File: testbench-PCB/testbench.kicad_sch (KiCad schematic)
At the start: 0 parts

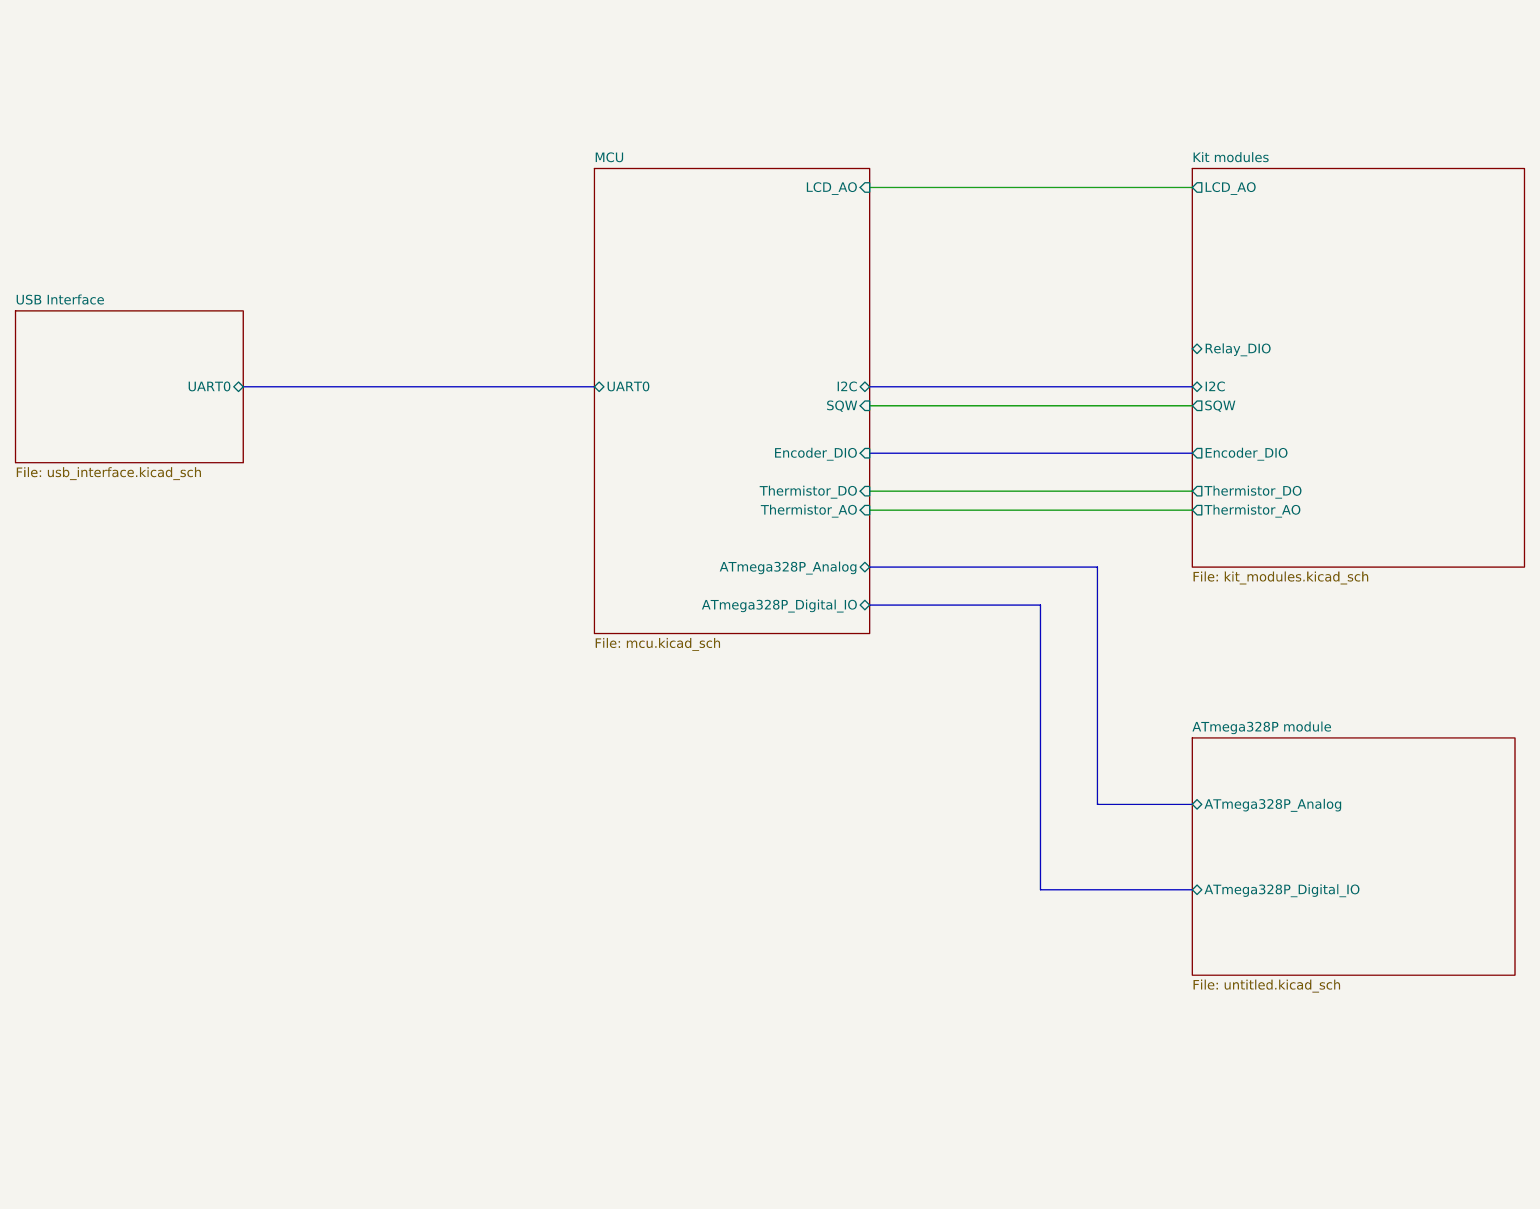
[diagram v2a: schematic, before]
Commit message: Finished connection between modules and MCU.
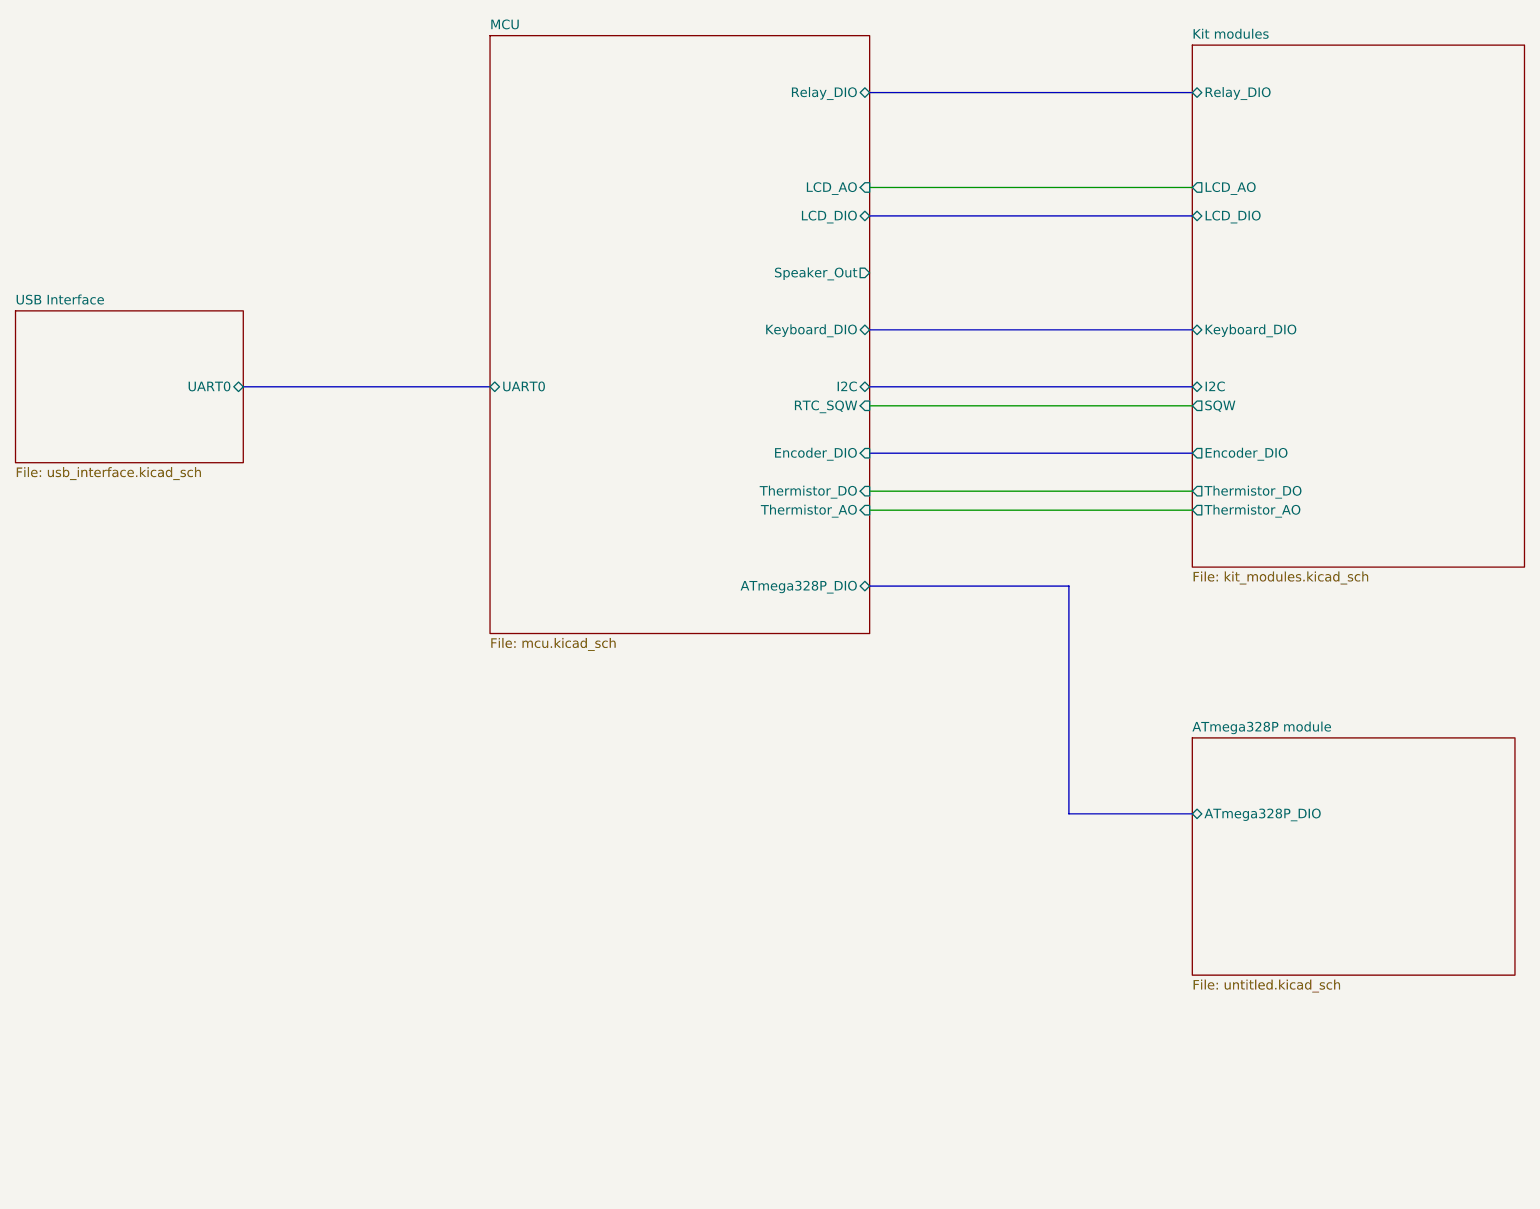
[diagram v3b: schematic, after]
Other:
- sheet ATmega328P module ports: added ATmega328P_DIO; removed ATmega328P_Analog, ATmega328P_Digital_IO
- sheet Kit modules ports: added Keyboard_DIO, LCD_DIO; removed none
- sheet MCU ports: added ATmega328P_DIO, Keyboard_DIO, LCD_DIO, RTC_SQW, Relay_DIO, Speaker_Out; removed ATmega328P_Analog, ATmega328P_Digital_IO, SQW
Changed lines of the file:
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@@
     (stroke (width 0) (type default))
   )
-  (bus (pts (xy 64.77 71.12) (xy 111.76 71.12))
+  (bus (pts (xy 175.26 128.27) (xy 191.77 128.27))
     (stroke (width 0) (type default))
   )
-  (bus (pts (xy 171.45 138.43) (xy 191.77 138.43))
+  (bus (pts (xy 64.77 71.12) (xy 97.79 71.12))
+    (stroke (width 0) (type default))
+  )
+  (bus (pts (xy 148.59 63.5) (xy 191.77 63.5))
     (stroke (width 0) (type default))
   )
@@
     (stroke (width 0) (type default))
   )
-  (bus (pts (xy 171.45 100.33) (xy 171.45 138.43))
-    (stroke (width 0) (type default))
-  )
-  (bus (pts (xy 148.59 95.25) (xy 179.07 95.25))
+  (bus (pts (xy 148.59 48.26) (xy 191.77 48.26))
     (stroke (width 0) (type default))
   )
   (wire (pts (xy 148.59 85.09) (xy 191.77 85.09))
-    (stroke (width 0) (type default))
-  )
-  (bus (pts (xy 179.07 95.25) (xy 179.07 127))
     (stroke (width 0) (type default))
   )
@@
     (stroke (width 0) (type default))
   )
-  (bus (pts (xy 179.07 127) (xy 191.77 127))
+  (bus (pts (xy 148.59 31.75) (xy 191.77 31.75))
+    (stroke (width 0) (type default))
+  )
+  (bus (pts (xy 175.26 97.79) (xy 175.26 128.27))
     (stroke (width 0) (type default))
   )
@@
     (stroke (width 0) (type default))
   )
-  (bus (pts (xy 148.59 100.33) (xy 171.45 100.33))
+  (bus (pts (xy 148.59 97.79) (xy 175.26 97.79))
     (stroke (width 0) (type default))
   )
-  (sheet (at 111.76 41.91) (size 36.83 62.23) (fields_autoplaced)
+  (sheet (at 97.79 24.13) (size 50.8 80.01) (fields_autoplaced)
     (stroke (width 0.1524) (type solid))
     (fill (color 255 229 191 1.0000))
-    (property "Sheetname" "MCU" (at 111.76 41.1984 0)
+    (property "Sheetname" "MCU" (at 97.79 23.4184 0)
       (effects (font (size 1.27 1.27)) (justify left bottom))
     )
-    (property "Sheetfile" "mcu.kicad_sch" (at 111.76 104.7246 0)
+    (property "Sheetfile" "mcu.kicad_sch" (at 97.79 104.7246 0)
       (effects (font (size 1.27 1.27)) (justify left top))
     )
-    (pin "UART0" bidirectional (at 111.76 71.12 180)
+    (pin "UART0" bidirectional (at 97.79 71.12 180)
       (effects (font (size 1.27 1.27)) (justify left))
     )
     (pin "I2C" bidirectional (at 148.59 71.12 0)
-      (effects (font (size 1.27 1.27)) (justify right))
-    )
-    (pin "SQW" input (at 148.59 73.66 0)
-      (effects (font (size 1.27 1.27)) (justify right))
-    )
-    (pin "ATmega328P_Analog" bidirectional (at 148.59 95.25 0)
-      (effects (font (size 1.27 1.27)) (justify right))
-    )
-    (pin "ATmega328P_Digital_IO" bidirectional (at 148.59 100.33 0)
       (effects (font (size 1.27 1.27)) (justify right))
     )
@@
     )
     (pin "Thermistor_DO" input (at 148.59 85.09 0)
+      (effects (font (size 1.27 1.27)) (justify right))
+    )
+    (pin "Keyboard_DIO" bidirectional (at 148.59 63.5 0)
+      (effects (font (size 1.27 1.27)) (justify right))
+    )
+    (pin "LCD_DIO" bidirectional (at 148.59 48.26 0)
+      (effects (font (size 1.27 1.27)) (justify right))
+    )
+    (pin "Speaker_Out" output (at 148.59 55.88 0)
+      (effects (font (size 1.27 1.27)) (justify right))
+    )
+    (pin "Relay_DIO" bidirectional (at 148.59 31.75 0)
+      (effects (font (size 1.27 1.27)) (justify right))
+    )
+    (pin "ATmega328P_DIO" bidirectional (at 148.59 97.79 0)
+      (effects (font (size 1.27 1.27)) (justify right))
+    )
+    (pin "RTC_SQW" input (at 148.59 73.66 0)
       (effects (font (size 1.27 1.27)) (justify right))
     )
@@
       (effects (font (size 1.27 1.27)) (justify left top))
     )
-    (pin "ATmega328P_Analog" bidirectional (at 191.77 127 180)
-      (effects (font (size 1.27 1.27)) (justify left))
-    )
-    (pin "ATmega328P_Digital_IO" bidirectional (at 191.77 138.43 180)
+    (pin "ATmega328P_DIO" bidirectional (at 191.77 128.27 180)
       (effects (font (size 1.27 1.27)) (justify left))
     )
@@
     )
   )
-  (sheet (at 191.77 41.91) (size 44.45 53.34) (fields_autoplaced)
+  (sheet (at 191.77 25.4) (size 44.45 69.85) (fields_autoplaced)
     (stroke (width 0.1524) (type solid))
     (fill (color 255 229 191 1.0000))
-    (property "Sheetname" "Kit modules" (at 191.77 41.1984 0)
+    (property "Sheetname" "Kit modules" (at 191.77 24.6884 0)
       (effects (font (size 1.27 1.27)) (justify left bottom))
     )
     (property "Sheetfile" "kit_modules.kicad_sch" (at 191.77 95.8346 0)
       (effects (font (size 1.27 1.27)) (justify left top))
-    )
-    (pin "Relay_DIO" bidirectional (at 191.77 66.04 180)
-      (effects (font (size 1.27 1.27)) (justify left))
     )
     (pin "I2C" bidirectional (at 191.77 71.12 180)
@@
       (effects (font (size 1.27 1.27)) (justify left))
     )
+    (pin "Keyboard_DIO" bidirectional (at 191.77 63.5 180)
+      (effects (font (size 1.27 1.27)) (justify left))
+    )
+    (pin "LCD_DIO" bidirectional (at 191.77 48.26 180)
+      (effects (font (size 1.27 1.27)) (justify left))
+    )
+    (pin "Relay_DIO" bidirectional (at 191.77 31.75 180)
+      (effects (font (size 1.27 1.27)) (justify left))
+    )

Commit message: Changed naming convention.
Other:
- sheet ATmega328P module ports: added DUT[0..20]; removed ATmega328P_DIO
- sheet Kit modules ports: added KEY_D[0..7], LCD_D[0..6], RTC_SQW, {Encoder_DIO}, {I2C}, {RELAY_IO}; removed Encoder_DIO, I2C, Keyboard_DIO, LCD_DIO, Relay_DIO, SQW
- sheet MCU ports: added DUT[0..20], KEY_D[0..7], LCD_D[0..6], {Encoder_DIO}, {I2C}, {RELAY_IO}, {UART0}; removed ATmega328P_DIO, Encoder_DIO, I2C, Keyboard_DIO, LCD_DIO, Relay_DIO, UART0
- sheet USB Interface ports: added {UART0}; removed UART0
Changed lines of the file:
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@@
 (kicad_sch (version 20230121) (generator eeschema)
   (paper "A4")
-  (bus (pts (xy 148.59 80.01) (xy 191.77 80.01))
+  (wire (pts (xy 191.77 74.93) (xy 148.59 74.93))
     (stroke (width 0) (type default))
   )
-  (bus (pts (xy 175.26 128.27) (xy 191.77 128.27))
+  (bus (pts (xy 148.59 50.8) (xy 191.77 50.8))
     (stroke (width 0) (type default))
   )
-  (bus (pts (xy 64.77 71.12) (xy 97.79 71.12))
+  (bus (pts (xy 148.59 43.815) (xy 191.77 43.815))
     (stroke (width 0) (type default))
   )
-  (bus (pts (xy 148.59 63.5) (xy 191.77 63.5))
+  (bus (pts (xy 148.59 97.79) (xy 170.18 97.79))
     (stroke (width 0) (type default))
   )
-  (wire (pts (xy 148.59 73.66) (xy 191.77 73.66))
+  (wire (pts (xy 148.59 35.56) (xy 191.77 35.56))
     (stroke (width 0) (type default))
   )
-  (bus (pts (xy 148.59 48.26) (xy 191.77 48.26))
+  (wire (pts (xy 148.59 80.645) (xy 191.77 80.645))
     (stroke (width 0) (type default))
   )
-  (wire (pts (xy 148.59 85.09) (xy 191.77 85.09))
+  (bus (pts (xy 64.77 74.93) (xy 97.79 74.93))
     (stroke (width 0) (type default))
   )
-  (wire (pts (xy 148.59 87.63) (xy 191.77 87.63))
+  (bus (pts (xy 170.18 128.27) (xy 191.77 128.27))
     (stroke (width 0) (type default))
   )
-  (wire (pts (xy 148.59 44.45) (xy 191.77 44.45))
+  (bus (pts (xy 170.18 97.79) (xy 170.18 128.27))
     (stroke (width 0) (type default))
   )
-  (bus (pts (xy 148.59 31.75) (xy 191.77 31.75))
+  (bus (pts (xy 148.59 67.945) (xy 191.77 67.945))
     (stroke (width 0) (type default))
   )
-  (bus (pts (xy 175.26 97.79) (xy 175.26 128.27))
+  (bus (pts (xy 148.59 57.15) (xy 191.77 57.15))
     (stroke (width 0) (type default))
   )
-  (bus (pts (xy 148.59 71.12) (xy 191.77 71.12))
+  (bus (pts (xy 191.77 90.17) (xy 148.59 90.17))
     (stroke (width 0) (type default))
   )
-  (bus (pts (xy 148.59 97.79) (xy 175.26 97.79))
+  (wire (pts (xy 148.59 33.02) (xy 191.77 33.02))
     (stroke (width 0) (type default))
   )
@@
       (effects (font (size 1.27 1.27)) (justify left top))
     )
-    (pin "UART0" bidirectional (at 97.79 71.12 180)
+    (pin "{UART0}" bidirectional (at 97.79 74.93 180)
       (effects (font (size 1.27 1.27)) (justify left))
     )
-    (pin "I2C" bidirectional (at 148.59 71.12 0)
+    (pin "LCD_D[0..6]" bidirectional (at 148.59 57.15 0)
       (effects (font (size 1.27 1.27)) (justify right))
     )
-    (pin "Encoder_DIO" input (at 148.59 80.01 0)
+    (pin "KEY_D[0..7]" bidirectional (at 148.59 50.8 0)
       (effects (font (size 1.27 1.27)) (justify right))
     )
-    (pin "LCD_AO" input (at 148.59 44.45 0)
+    (pin "{I2C}" bidirectional (at 148.59 43.815 0)
       (effects (font (size 1.27 1.27)) (justify right))
     )
-    (pin "Thermistor_AO" input (at 148.59 87.63 0)
+    (pin "Speaker_Out" output (at 148.59 28.575 0)
       (effects (font (size 1.27 1.27)) (justify right))
     )
-    (pin "Thermistor_DO" input (at 148.59 85.09 0)
+    (pin "{RELAY_IO}" bidirectional (at 148.59 67.945 0)
       (effects (font (size 1.27 1.27)) (justify right))
     )
-    (pin "Keyboard_DIO" bidirectional (at 148.59 63.5 0)
+    (pin "RTC_SQW" input (at 148.59 80.645 0)
       (effects (font (size 1.27 1.27)) (justify right))
     )
-    (pin "LCD_DIO" bidirectional (at 148.59 48.26 0)
+    (pin "DUT[0..20]" bidirectional (at 148.59 97.79 0)
       (effects (font (size 1.27 1.27)) (justify right))
     )
-    (pin "Speaker_Out" output (at 148.59 55.88 0)
+    (pin "{Encoder_DIO}" input (at 148.59 90.17 0)
       (effects (font (size 1.27 1.27)) (justify right))
     )
-    (pin "Relay_DIO" bidirectional (at 148.59 31.75 0)
+    (pin "Thermistor_DO" input (at 148.59 33.02 0)
       (effects (font (size 1.27 1.27)) (justify right))
     )
-    (pin "ATmega328P_DIO" bidirectional (at 148.59 97.79 0)
+    (pin "Thermistor_AO" input (at 148.59 35.56 0)
       (effects (font (size 1.27 1.27)) (justify right))
     )
-    (pin "RTC_SQW" input (at 148.59 73.66 0)
+    (pin "LCD_AO" input (at 148.59 74.93 0)
       (effects (font (size 1.27 1.27)) (justify right))
     )
@@
       (effects (font (size 1.27 1.27)) (justify left top))
     )
-    (pin "ATmega328P_DIO" bidirectional (at 191.77 128.27 180)
+    (pin "DUT[0..20]" bidirectional (at 191.77 128.27 180)
       (effects (font (size 1.27 1.27)) (justify left))
     )
@@
       (effects (font (size 1.27 1.27)) (justify left top))
     )
-    (pin "I2C" bidirectional (at 191.77 71.12 180)
+    (pin "LCD_D[0..6]" bidirectional (at 191.77 57.15 180)
       (effects (font (size 1.27 1.27)) (justify left))
     )
-    (pin "SQW" output (at 191.77 73.66 180)
+    (pin "KEY_D[0..7]" bidirectional (at 191.77 50.8 180)
       (effects (font (size 1.27 1.27)) (justify left))
     )
-    (pin "Encoder_DIO" output (at 191.77 80.01 180)
+    (pin "LCD_AO" output (at 191.77 74.93 180)
       (effects (font (size 1.27 1.27)) (justify left))
     )
-    (pin "Thermistor_DO" output (at 191.77 85.09 180)
+    (pin "Thermistor_DO" output (at 191.77 33.02 180)
       (effects (font (size 1.27 1.27)) (justify left))
     )
-    (pin "Thermistor_AO" output (at 191.77 87.63 180)
+    (pin "Thermistor_AO" output (at 191.77 35.56 180)
       (effects (font (size 1.27 1.27)) (justify left))
     )
-    (pin "LCD_AO" output (at 191.77 44.45 180)
+    (pin "{RELAY_IO}" bidirectional (at 191.77 67.945 180)
       (effects (font (size 1.27 1.27)) (justify left))
     )
-    (pin "Keyboard_DIO" bidirectional (at 191.77 63.5 180)
+    (pin "{Encoder_DIO}" output (at 191.77 90.17 180)
       (effects (font (size 1.27 1.27)) (justify left))
     )
-    (pin "LCD_DIO" bidirectional (at 191.77 48.26 180)
+    (pin "{I2C}" bidirectional (at 191.77 43.815 180)
       (effects (font (size 1.27 1.27)) (justify left))
     )
-    (pin "Relay_DIO" bidirectional (at 191.77 31.75 180)
+    (pin "RTC_SQW" output (at 191.77 80.645 180)
       (effects (font (size 1.27 1.27)) (justify left))
     )
@@
       (effects (font (size 1.27 1.27)) (justify left top))
     )
-    (pin "UART0" bidirectional (at 64.77 71.12 0)
+    (pin "{UART0}" bidirectional (at 64.77 74.93 0)
       (effects (font (size 1.27 1.27)) (justify right))
     )
